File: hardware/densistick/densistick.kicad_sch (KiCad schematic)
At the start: 57 parts, among them J1 Cable, SW1 SW_Push, U1 TSL2585, U2 USBLC6-2SC6, U3 MIC4812, U4 FT260Q, U5 MIC5365-1.8YC5, U6 CAT24C08, U7 MCP4017-104E/LT

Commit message: Various bits of TVS and layout cleanup for the meter probe and DensiStick
Decided to standardize on the new TI ESD321 TVS diode for single-line
protection on these boards. This part appears designed for this use,
especially with a lower working voltage. Its also in a similar package
to the Semtech part previously being used in some of these cases.

Created a new SOD-523 footprint based on TI's recommended land pattern,
which might work a little better than the stock one.

Updated the DensiStick to use the same 4.7uF MLCC for the bulk input
capacitor as the meter probe.

Various other minor tweaks to the fab layers and traces associated with
the above changes.
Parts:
- removed C6: 4.7uF, Capacitor_Tantalum_SMD:CP_EIA-3216-18_Kemet-A, symbol Device:C_Polarized_Small
- removed D5: uClamp0501H, Diode_SMD:D_SOD-523, symbol Project:uClamp3301H
- added C6: 4.7uF, Capacitor_SMD:C_0603_1608Metric, symbol Device:C_Small
- added D5: ESD321, lib_fp:D_TI_SOD-523_DYA0002A, symbol Device:D_Zener
- FB1: value 600R@100MHz -> 600R; Manufacturer TDK Corporation -> Würth Elektronik; Manufacturer PN MMZ1608R601ATD25 -> 742792651; Supplier PN 445-MMZ1608R601ATD25CT-ND -> 732-1593-1-ND
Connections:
- net +5V: now also C6.1
- net Earth: now also D5.2 (A)
- net GND: now also C6.2
- net at R3.1, SW1.2: now also D5.1 (K)

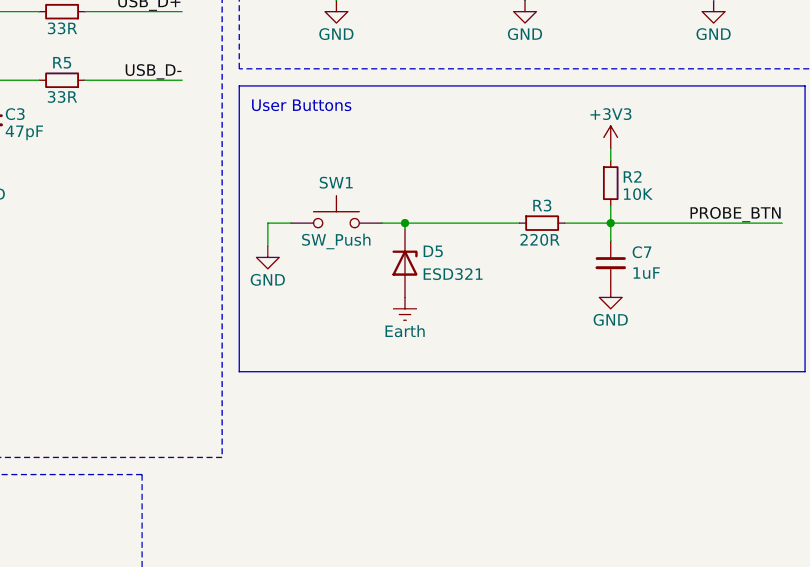
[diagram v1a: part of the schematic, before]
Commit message: Update ESD diode symbols and footprints
Fix #78
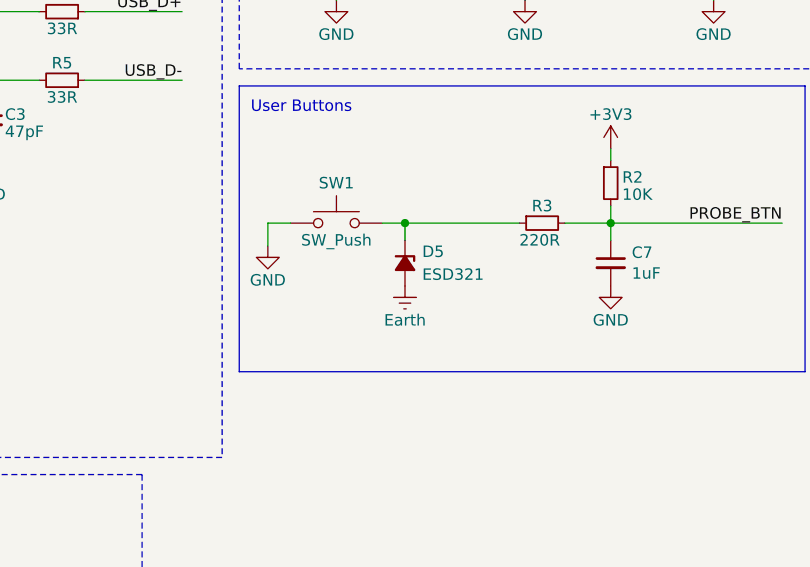
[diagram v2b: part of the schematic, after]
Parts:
- D5: symbol Device:D_Zener -> Project:ESD321DYAR
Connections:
- net Earth: now also D5.1 (A); no longer D5.2 (A)
- net at R3.1, SW1.2: now also D5.2 (K); no longer D5.1 (K)
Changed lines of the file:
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@@
 	(wire
 		(pts
-			(xy 147.32 128.905) (xy 147.32 128.27)
+			(xy 147.32 128.27) (xy 147.32 130.175)
 		)
 		(stroke
@@
 	(symbol
 		(lib_id "power:Earth")
-		(at 147.32 136.525 0)
+		(at 147.32 135.255 0)
 		(mirror y)
 		(unit 1)
@@
 		(fields_autoplaced yes)
 		(property "Reference" "#PWR050"
-			(at 147.32 142.875 0)
+			(at 147.32 141.605 0)
 			(effects
 				(font
@@
 		)
 		(property "Value" "Earth"
-			(at 147.32 140.335 0)
+			(at 147.32 139.065 0)
 			(effects
 				(font
@@
 		)
 		(property "Footprint" ""
-			(at 147.32 136.525 0)
+			(at 147.32 135.255 0)
 			(effects
 				(font
@@
 		)
 		(property "Datasheet" "~"
-			(at 147.32 136.525 0)
+			(at 147.32 135.255 0)
 			(effects
 				(font
@@
 		)
 		(property "Description" "Power symbol creates a global label with name \"Earth\""
-			(at 147.32 136.525 0)
+			(at 147.32 135.255 0)
 			(effects
 				(font
@@
 		)
 		(property "Manufacturer" ""
-			(at 147.32 136.525 0)
+			(at 147.32 135.255 0)
 			(effects
 				(font
@@
 		)
 		(property "Manufacturer PN" ""
-			(at 147.32 136.525 0)
+			(at 147.32 135.255 0)
 			(effects
 				(font
@@
 		)
 		(property "Supplier" ""
-			(at 147.32 136.525 0)
+			(at 147.32 135.255 0)
 			(effects
 				(font
@@
 		)
 		(property "Supplier PN" ""
-			(at 147.32 136.525 0)
+			(at 147.32 135.255 0)
 			(effects
 				(font
@@
 	)
 	(symbol
-		(lib_id "Device:D_Zener")
+		(lib_id "Project:ESD321DYAR")
 		(at 147.32 132.715 270)
 		(unit 1)
@@
 		)
 		(property "Footprint" "lib_fp:D_TI_SOD-523_DYA0002A"
-			(at 147.32 132.715 0)
+			(at 139.446 132.715 0)
 			(effects
 				(font
@@
 			)
 		)
-		(property "Datasheet" "https://www.ti.com/lit/ds/slvsen8b/slvsen8b.pdf"
-			(at 147.32 132.715 0)
+		(property "Datasheet" "https://www.ti.com/lit/ds/symlink/esd321.pdf"
+			(at 136.906 132.715 0)
 			(effects
 				(font
@@
 		)
 		(property "Description" "TVS DIODE 3.6VWM 6.3VC SOD523"
-			(at 147.32 132.715 0)
+			(at 141.986 132.715 0)
 			(effects
 				(font

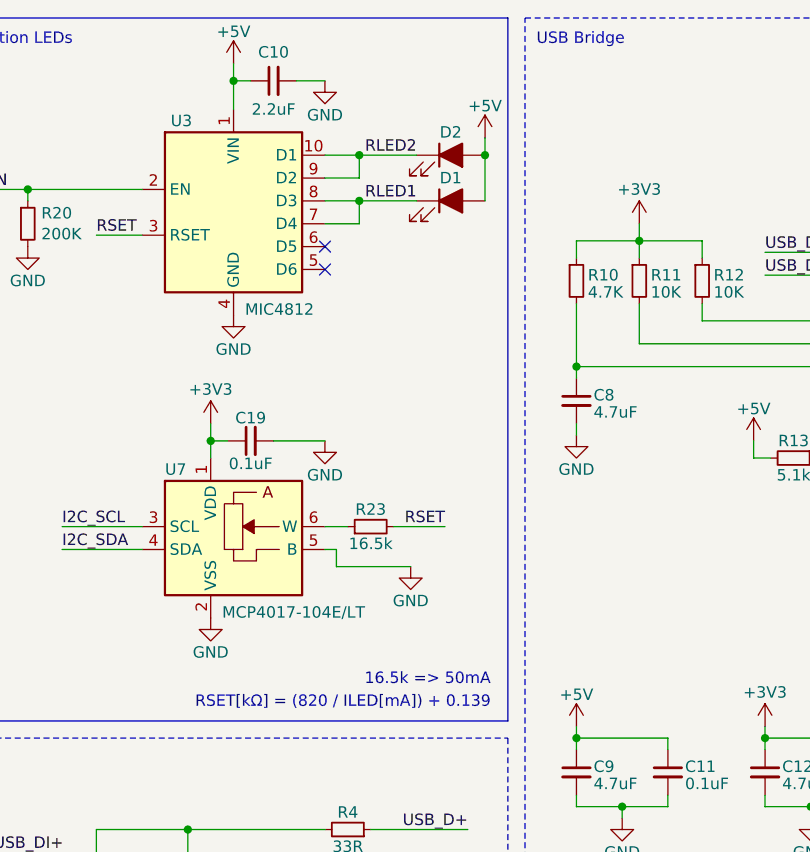
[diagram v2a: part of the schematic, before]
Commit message: Change DensiStick LED driver wiring
Halve the value of the LED driver's RSET resistor, and change the LED
wiring so that channels aren't doubled.  This effect of this should be
keeping the maximum LED current the same, while halving the minimum LED
current.

Fix #80
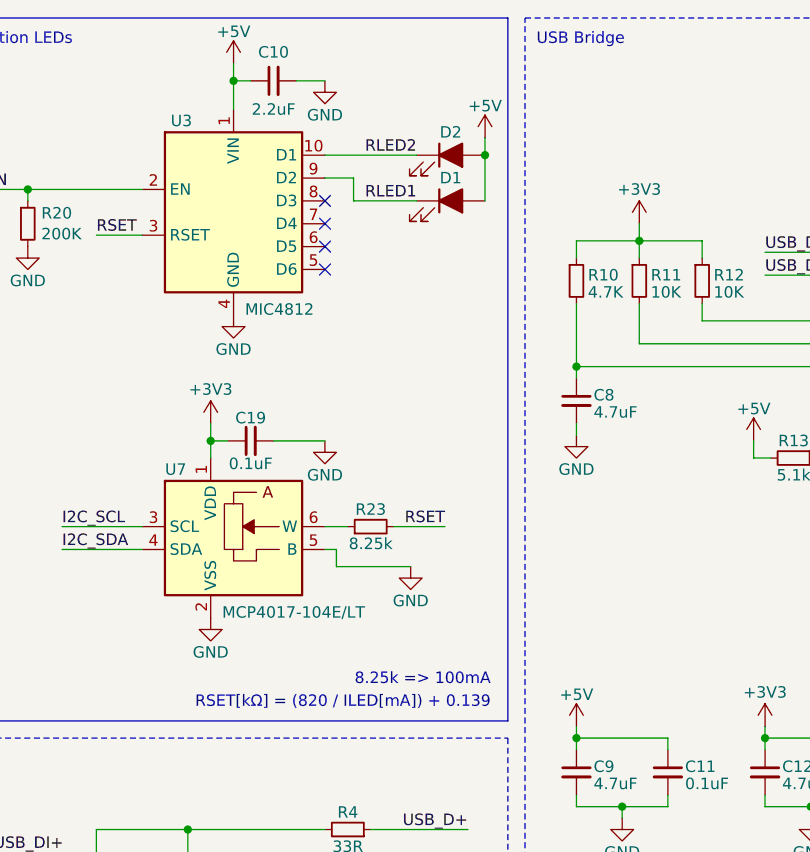
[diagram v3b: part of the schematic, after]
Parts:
- R23: value 16.5k -> 8.25k; Manufacturer TE Connectivity Passive Product -> Vishay Dale; Manufacturer PN CPF0603F16K5C1 -> CRCW06038K25FKEBC; Supplier Digi-Key -> Mouser; Supplier PN A102224CT-ND -> 71-CRCW06038K25FKEBC
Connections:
- net RLED1: now also U3.9 (D2); no longer U3.7 (D4), U3.8 (D3)
- net RLED2: no longer U3.9 (D2)
- no-connect marks 14 -> 16
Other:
- note added: "8.25k => 100mA"
- note removed: "16.5k => 50mA"
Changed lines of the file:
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@@
 	)
 	(junction
-		(at 110.49 34.925)
-		(diameter 0)
-		(color 0 0 0 0)
-	)
-	(junction
 		(at 73.66 33.655)
 		(diameter 0)
@@
 	)
 	(junction
-		(at 110.49 29.845)
-		(diameter 0)
-		(color 0 0 0 0)
-	)
-	(junction
 		(at 32.385 114.935)
 		(diameter 0)
@@
 	)
 	(no_connect
+		(at 106.68 37.465)
+	)
+	(no_connect
 		(at 165.735 55.88)
 	)
@@
 	)
 	(no_connect
+		(at 106.68 34.925)
+	)
+	(no_connect
 		(at 41.275 53.34)
 	)
@@
 	(wire
 		(pts
-			(xy 110.49 29.845) (xy 116.84 29.845)
+			(xy 106.68 29.845) (xy 116.84 29.845)
 		)
 		(stroke
@@
 	(wire
 		(pts
-			(xy 106.68 29.845) (xy 110.49 29.845)
-		)
-		(stroke
-			(width 0)
-			(type default)
-		)
-	)
-	(wire
-		(pts
 			(xy 75.565 175.895) (xy 75.565 178.435)
 		)
@@
 	(wire
 		(pts
-			(xy 110.49 37.465) (xy 110.49 34.925)
-		)
-		(stroke
-			(width 0)
-			(type default)
-		)
-	)
-	(wire
-		(pts
 			(xy 29.845 25.4) (xy 29.845 35.56)
 		)
@@
 	(wire
 		(pts
-			(xy 106.68 37.465) (xy 110.49 37.465)
-		)
-		(stroke
-			(width 0)
-			(type default)
-		)
-	)
-	(wire
-		(pts
 			(xy 63.5 33.655) (xy 73.66 33.655)
 		)
@@
 	(wire
 		(pts
-			(xy 141.605 50.8) (xy 141.605 46.355)
+			(xy 109.855 32.385) (xy 106.68 32.385)
 		)
 		(stroke
@@
 	(wire
 		(pts
-			(xy 144.78 100.965) (xy 144.78 102.235)
+			(xy 141.605 50.8) (xy 141.605 46.355)
 		)
 		(stroke
@@
 	(wire
 		(pts
-			(xy 107.95 75.565) (xy 116.205 75.565)
+			(xy 144.78 100.965) (xy 144.78 102.235)
 		)
 		(stroke
@@
 	(wire
 		(pts
-			(xy 110.49 29.845) (xy 110.49 32.385)
+			(xy 107.95 75.565) (xy 116.205 75.565)
 		)
 		(stroke
@@
 	(wire
 		(pts
-			(xy 106.68 34.925) (xy 110.49 34.925)
-		)
-		(stroke
-			(width 0)
-			(type default)
-		)
-	)
-	(wire
-		(pts
 			(xy 165.1 128.27) (xy 170.18 128.27)
 		)
@@
 	(wire
 		(pts
-			(xy 110.49 34.925) (xy 116.84 34.925)
+			(xy 109.855 34.925) (xy 116.84 34.925)
 		)
 		(stroke
@@
 	(wire
 		(pts
+			(xy 109.855 34.925) (xy 109.855 32.385)
+		)
+		(stroke
+			(width 0)
+			(type default)
+		)
+	)
+	(wire
+		(pts
 			(xy 156.21 63.5) (xy 154.305 63.5)
 		)
@@
 	(wire
 		(pts
-			(xy 106.68 32.385) (xy 110.49 32.385)
-		)
-		(stroke
-			(width 0)
-			(type default)
-		)
-	)
-	(wire
-		(pts
 			(xy 147.32 128.27) (xy 147.32 130.175)
 		)
@@
 		)
 	)
-	(text "16.5k => 50mA"
+	(text "8.25k => 100mA"
 		(exclude_from_sim no)
 		(at 125.095 88.9 0)
@@
 	(symbol
 		(lib_id "Device:R_Small")
-		(at 111.76 71.12 90)
-		(unit 1)
-		(exclude_from_sim no)
-		(in_bom yes)
-		(on_board yes)
-		(dnp no)
-		(property "Reference" "R23"
-			(at 111.76 69.215 90)
-			(effects
-				(font
-					(size 1.27 1.27)
-				)
-			)
-		)
-		(property "Value" "16.5k"
-			(at 111.76 73.025 90)
-			(effects
-				(font
-					(size 1.27 1.27)
-				)
-			)
-		)
-		(property "Footprint" "Resistor_SMD:R_0603_1608Metric"
-			(at 111.76 71.12 0)
-			(effects
-				(font
-					(size 1.27 1.27)
-				)
-				(hide yes)
-			)
-		)
-		(property "Datasheet" "https://www.te.com/commerce/DocumentDelivery/DDEController?Action=srchrtrv&DocNm=1773200&DocType=DS&DocLang=English"
-			(at 111.76 71.12 0)
-			(effects
-				(font
-					(size 1.27 1.27)
-				)
-				(hide yes)
-			)
-		)
-		(property "Description" "RES SMD 16.5K OHM 1% 1/16W 0603"
-			(at 111.76 71.12 0)
-			(effects
-				(font
-					(size 1.27 1.27)
-				)
-				(hide yes)
-			)
-		)
-		(property "Manufacturer" "TE Connectivity Passive Product"
-			(at 111.76 71.12 0)
-			(effects
-				(font
-					(size 1.27 1.27)
-				)
-				(hide yes)
-			)
-		)
-		(property "Manufacturer PN" "CPF0603F16K5C1"
-			(at 111.76 71.12 0)
-			(effects
-				(font
-					(size 1.27 1.27)
-				)
-				(hide yes)
-			)
-		)
-		(property "Supplier" "Digi-Key"
-			(at 111.76 71.12 0)
-			(effects
-				(font
-					(size 1.27 1.27)
-				)
-				(hide yes)
-			)
-		)
-		(property "Supplier PN" "A102224CT-ND"
-			(at 111.76 71.12 0)
-			(effects
-				(font
-					(size 1.27 1.27)
-				)
-				(hide yes)
-			)
-		)
-		(pin "1"
-		)
-		(pin "2"
-		)
-		(instances
-			(project "densistick"
-				(path "/8d0c1d66-35ef-4a53-a28f-436a11b54f42"
-					(reference "R23")
-					(unit 1)
-				)
-			)
-		)
-	)
-	(symbol
-		(lib_id "Device:R_Small")
 		(at 73.66 37.465 0)
 		(unit 1)
@@
 					(unit 1)
 				)
+			)
+		)
+	)
+	(symbol
+		(lib_id "Device:R_Small")
+		(at 111.76 71.12 90)
+		(unit 1)
+		(exclude_from_sim no)
+		(in_bom yes)
+		(on_board yes)
+		(dnp no)
+		(property "Reference" "R23"
+			(at 111.76 69.215 90)
+			(effects
+				(font
+					(size 1.27 1.27)
+				)
+			)
+		)
+		(property "Value" "8.25k"
+			(at 111.76 73.025 90)
+			(effects
+				(font
+					(size 1.27 1.27)
+				)
+			)
+		)
+		(property "Footprint" "Resistor_SMD:R_0603_1608Metric"
+			(at 111.76 71.12 0)
+			(effects
+				(font
+					(size 1.27 1.27)
+				)
+				(hide yes)
+			)
+		)
+		(property "Datasheet" "https://www.vishay.com/docs/28773/crcwce3.pdf"
+			(at 111.76 71.12 0)
+			(effects
+				(font
+					(size 1.27 1.27)
+				)
+				(hide yes)
+			)
+		)
+		(property "Description" "RES SMD 8.25K OHM 1% 1/16W 0603"
+			(at 111.76 71.12 0)
+			(effects
+				(font
+					(size 1.27 1.27)
+				)
+				(hide yes)
+			)
+		)
+		(property "Manufacturer" "Vishay Dale"
+			(at 111.76 71.12 0)
+			(effects
+				(font
+					(size 1.27 1.27)
+				)
+				(hide yes)
+			)
+		)
+		(property "Manufacturer PN" "CRCW06038K25FKEBC"
+			(at 111.76 71.12 0)
+			(effects
+				(font
+					(size 1.27 1.27)
+				)
+				(hide yes)
+			)
+		)
+		(property "Supplier" "Mouser"
+			(at 111.76 71.12 0)
+			(effects
+				(font
+					(size 1.27 1.27)
+				)
+				(hide yes)
+			)
+		)
+		(property "Supplier PN" "71-CRCW06038K25FKEBC"
+			(at 111.76 71.12 0)
+			(effects
+				(font
+					(size 1.27 1.27)
+				)
+				(hide yes)
+			)
+		)
+		(pin "1"
+		)
+		(pin "2"
+		)
+		(instances
+			(project "densistick"
+				(path "/8d0c1d66-35ef-4a53-a28f-436a11b54f42"
+					(reference "R23")
+					(unit 1)
+				)

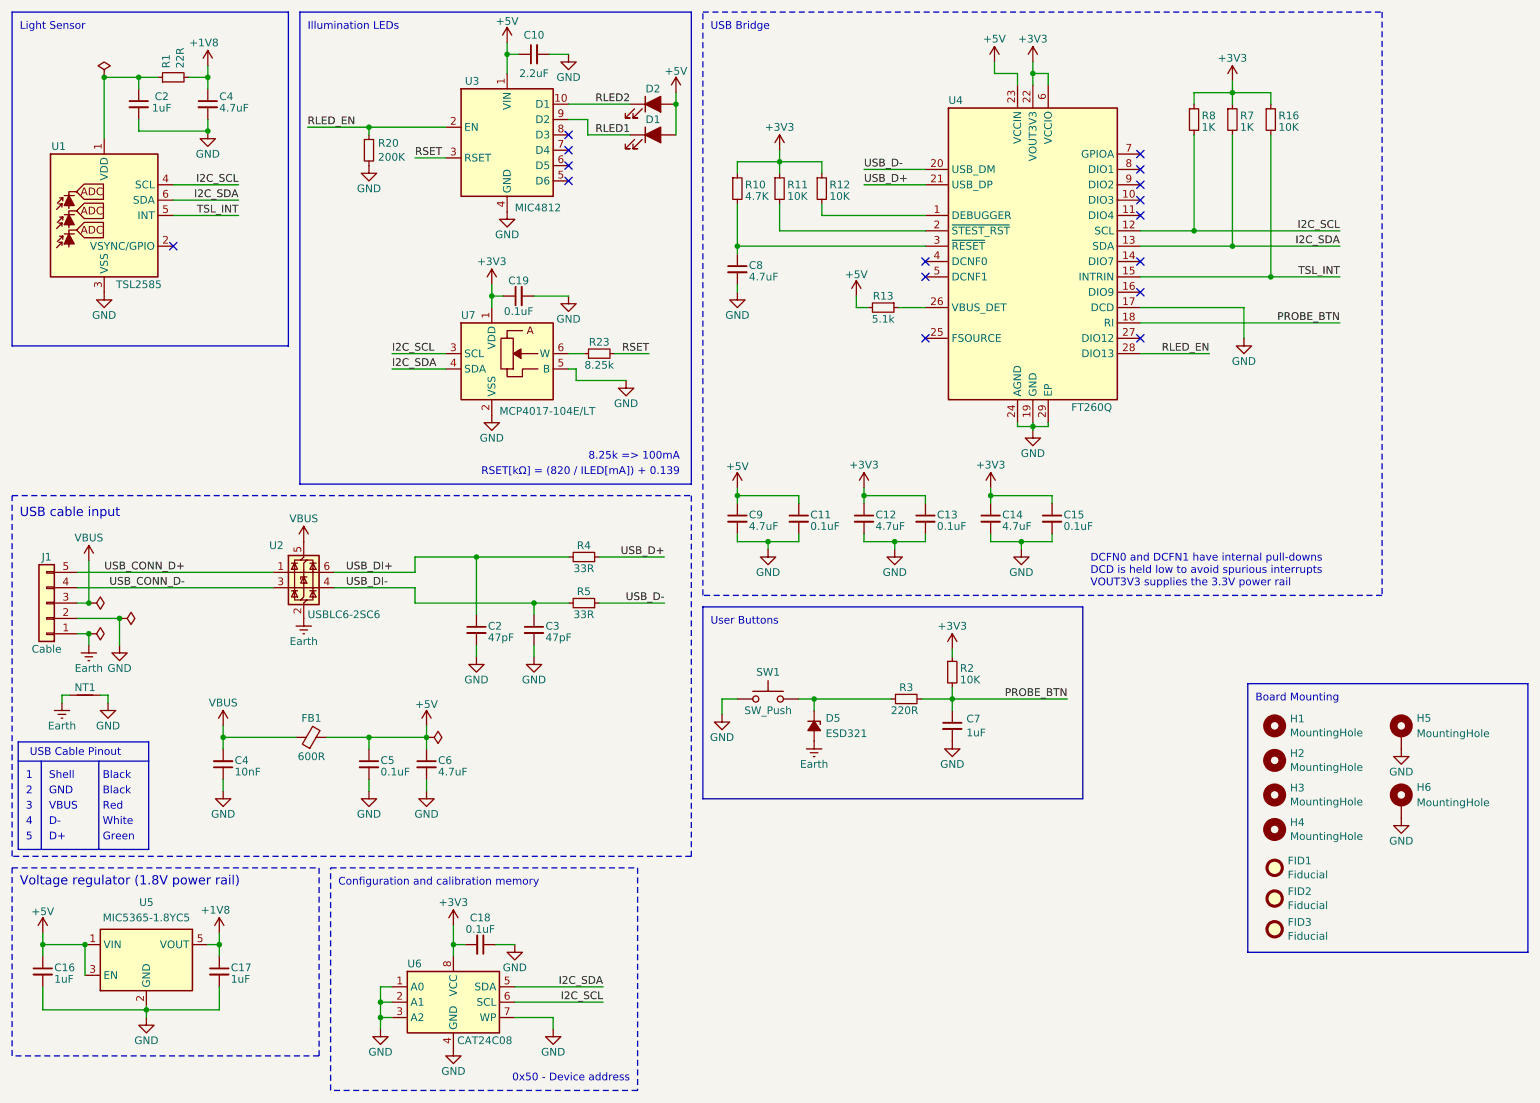
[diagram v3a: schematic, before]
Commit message: Route VSYNC to FT260 GPIOA on DensiStick
This makes the sensor-to-bridge connection on the DensiStick logically
match the same from the Meter Probe, and makes it possible to experiment
with using VSYNC as a trigger.

Doing this may be useful to provide more ways of operating the sensor,
and doesn't hurt if not used.

More routing cleanup may be necessary before this design is considered
complete.
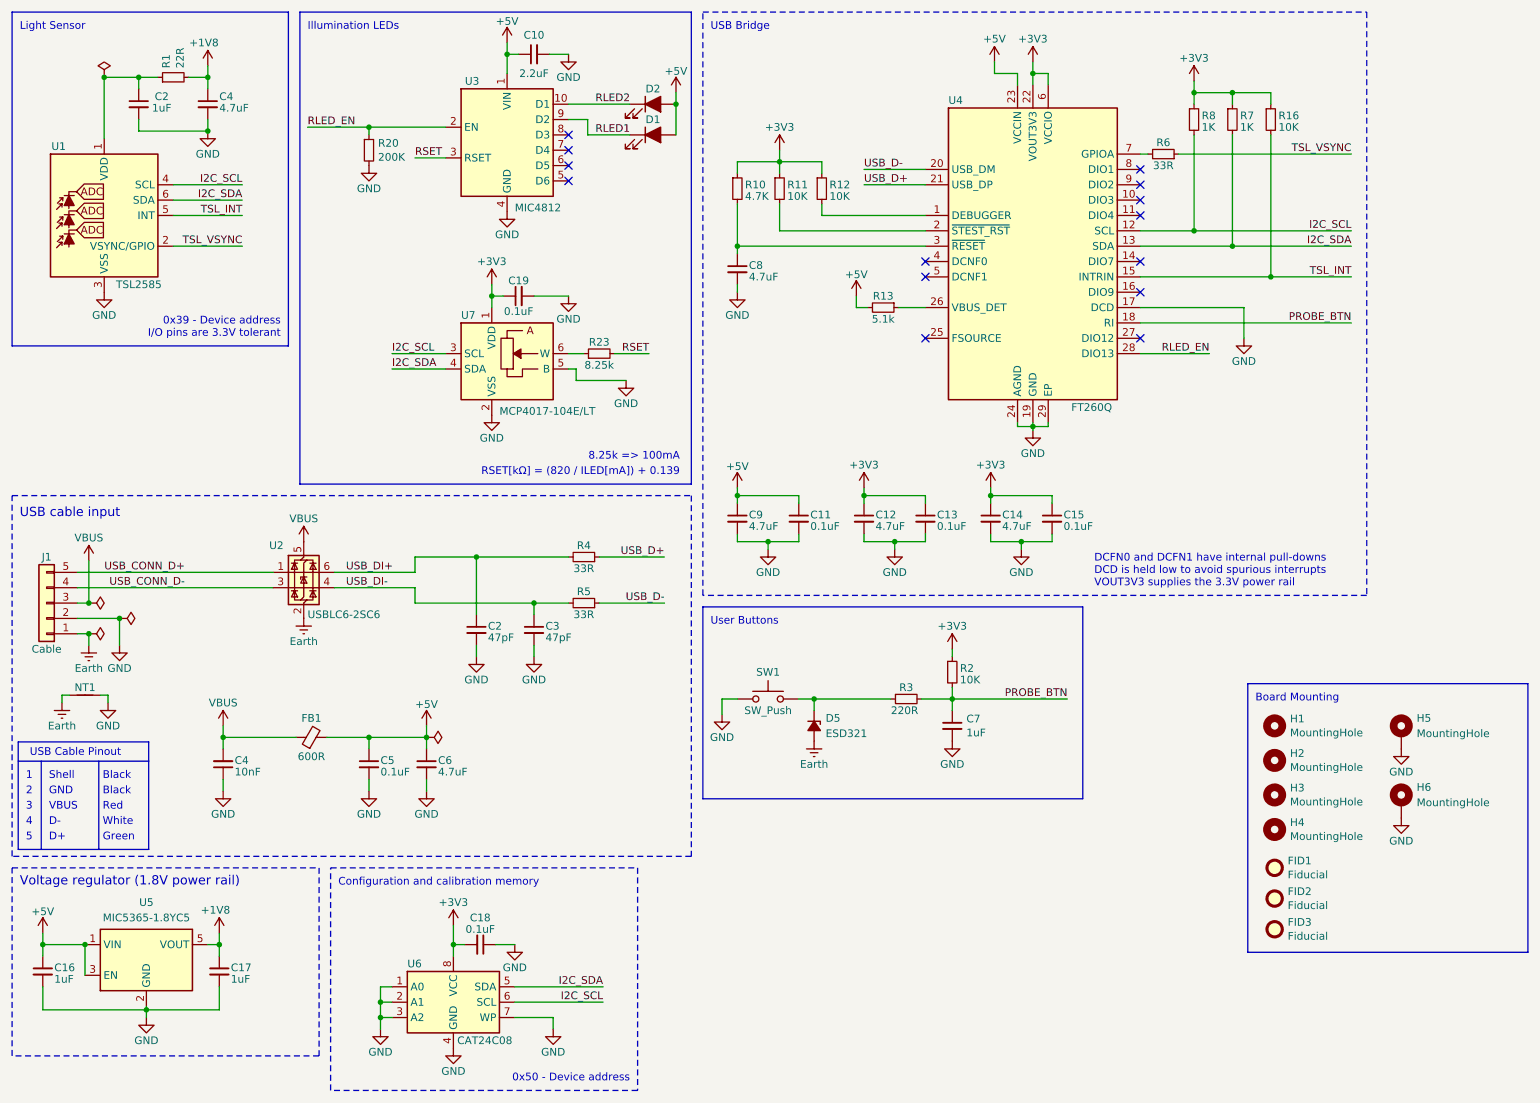
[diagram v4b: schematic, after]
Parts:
- added R6: 33R, Resistor_SMD:R_0603_1608Metric, symbol Device:R_Small
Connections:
- net TSL_VSYNC: now reaches U1.2 (VSYNC/GPIO)
- net TSL_VSYNC: now also R6.1
- net at U4.7 (DIO0): now also R6.2
- no-connect marks 16 -> 14
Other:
- note added: "0x39 - Device address I/O pins are 3.3V tolerant"

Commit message: Finalize DensiStick Rev B 2024-12-03
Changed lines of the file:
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@@
 	(title_block
 		(title "Printalyzer DensiStick")
-		(date "2024-11-24")
+		(date "2024-12-03")
 		(rev "B")
 		(company "Dektronics, Inc.")
@@
 		)
 		(pin "28"
+			(alternate "GPIOH")
 		)
 		(pin "27"
